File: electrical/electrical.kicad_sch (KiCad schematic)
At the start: 0 parts

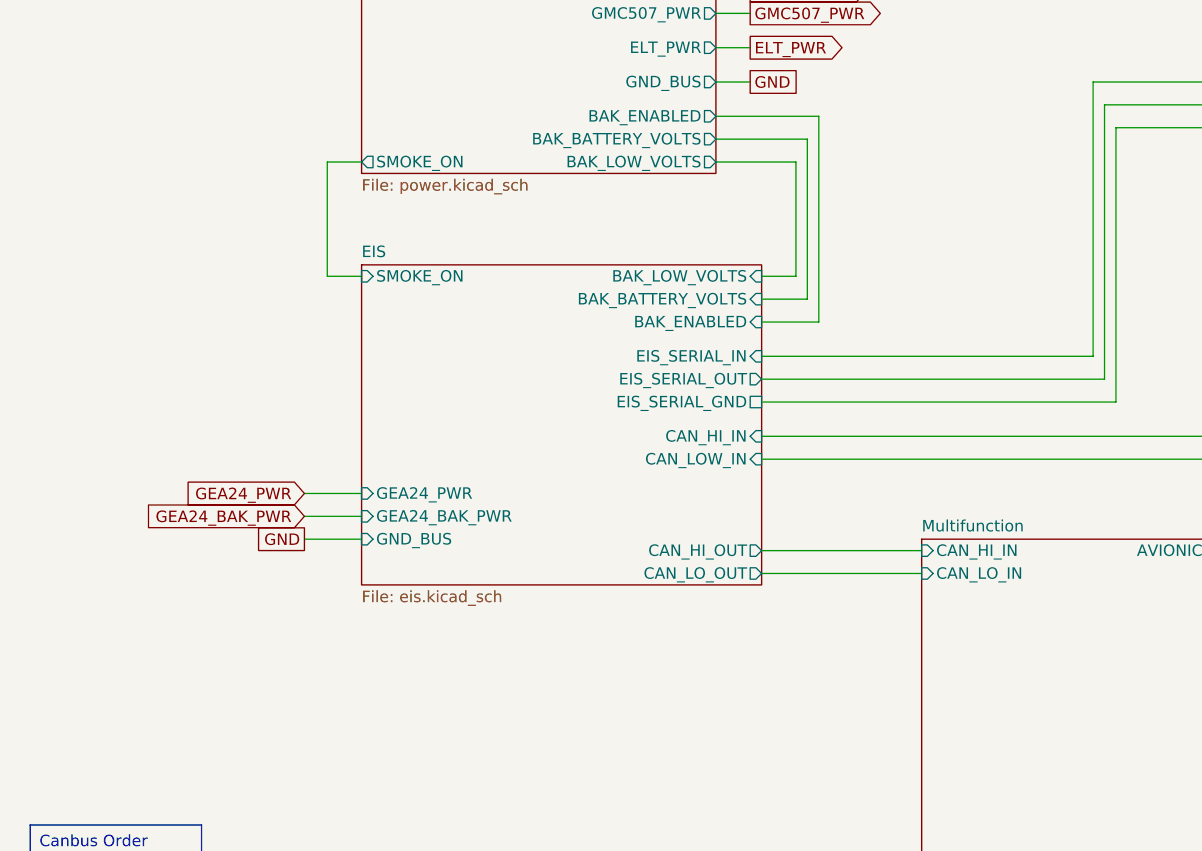
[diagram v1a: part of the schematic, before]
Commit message: Added Warning/Caution lights/buttons. Moved smoke on to GAD 27. Added glide button to GAD 27. Added lighting switched pots to GEA 24.
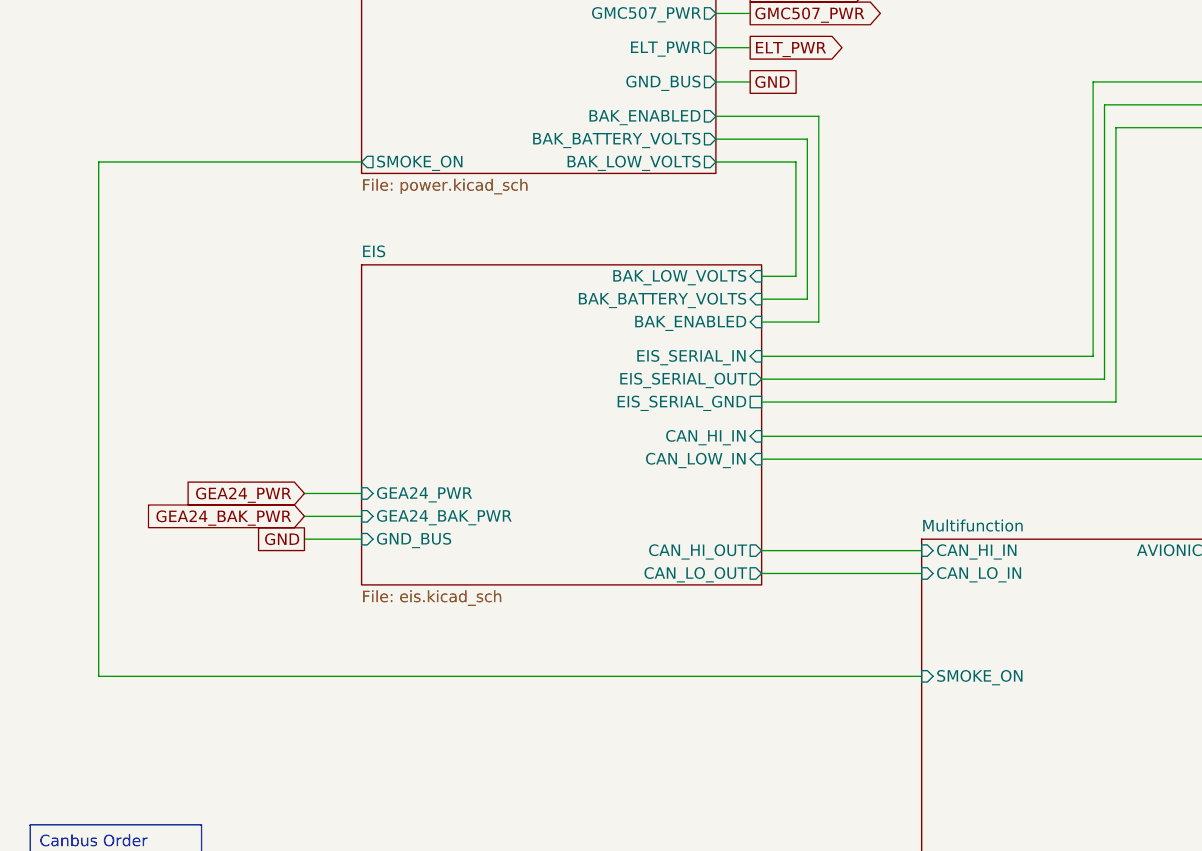
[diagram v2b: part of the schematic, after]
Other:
- sheet EIS ports: added none; removed SMOKE_ON
- sheet Multifunction ports: added SMOKE_ON; removed none
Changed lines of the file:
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@@
     (stroke (width 0) (type default))
   )
-  (wire (pts (xy 53.34 119.38) (xy 49.53 119.38))
+  (wire (pts (xy 24.13 119.38) (xy 53.34 119.38))
     (stroke (width 0) (type default))
   )
@@
     (stroke (width 0) (type default))
   )
-  (wire (pts (xy 49.53 119.38) (xy 49.53 132.08))
-    (stroke (width 0) (type default))
-  )
   (wire (pts (xy 134.62 110.49) (xy 173.99 110.49))
     (stroke (width 0) (type default))
@@
     (stroke (width 0) (type default))
   )
+  (wire (pts (xy 24.13 176.53) (xy 24.13 119.38))
+    (stroke (width 0) (type default))
+  )
   (wire (pts (xy 389.89 181.61) (xy 346.71 181.61))
     (stroke (width 0) (type default))
@@
     (stroke (width 0) (type default))
   )
+  (wire (pts (xy 115.57 176.53) (xy 24.13 176.53))
+    (stroke (width 0) (type default))
+  )
   (wire (pts (xy 92.71 87.63) (xy 96.52 87.63))
     (stroke (width 0) (type default))
@@
   )
   (wire (pts (xy 220.98 107.95) (xy 257.81 107.95))
-    (stroke (width 0) (type default))
-  )
-  (wire (pts (xy 49.53 132.08) (xy 53.34 132.08))
     (stroke (width 0) (type default))
   )
@@
       (effects (font (size 1.27 1.27)) (justify right))
     )
+    (pin "SMOKE_ON" input (at 115.57 176.53 180)
+      (effects (font (size 1.27 1.27)) (justify left))
+    )
     (instances
       (project "electrical"
@@
       (effects (font (size 1.27 1.27)) (justify right))
     )
-    (pin "SMOKE_ON" input (at 53.34 132.08 180)
-      (effects (font (size 1.27 1.27)) (justify left))
-    )
     (pin "EIS_SERIAL_OUT" output (at 97.79 143.51 0)

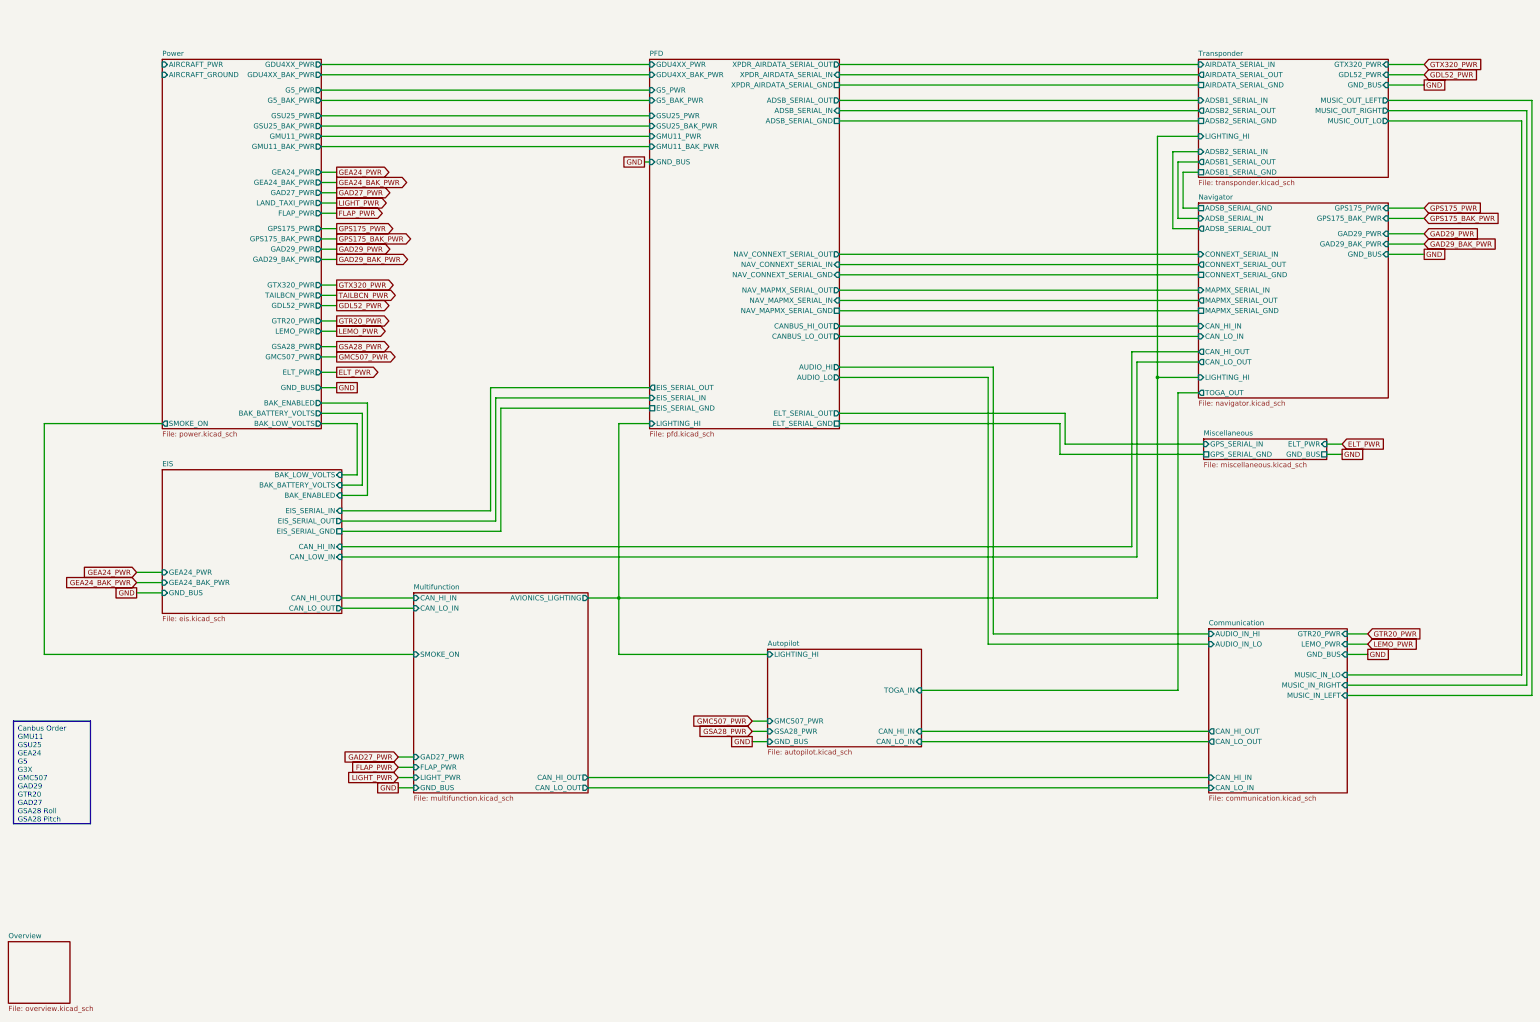
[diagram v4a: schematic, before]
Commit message: Updated electrical to not use IBBS. Also, added BT adapter and 3P3T switch.
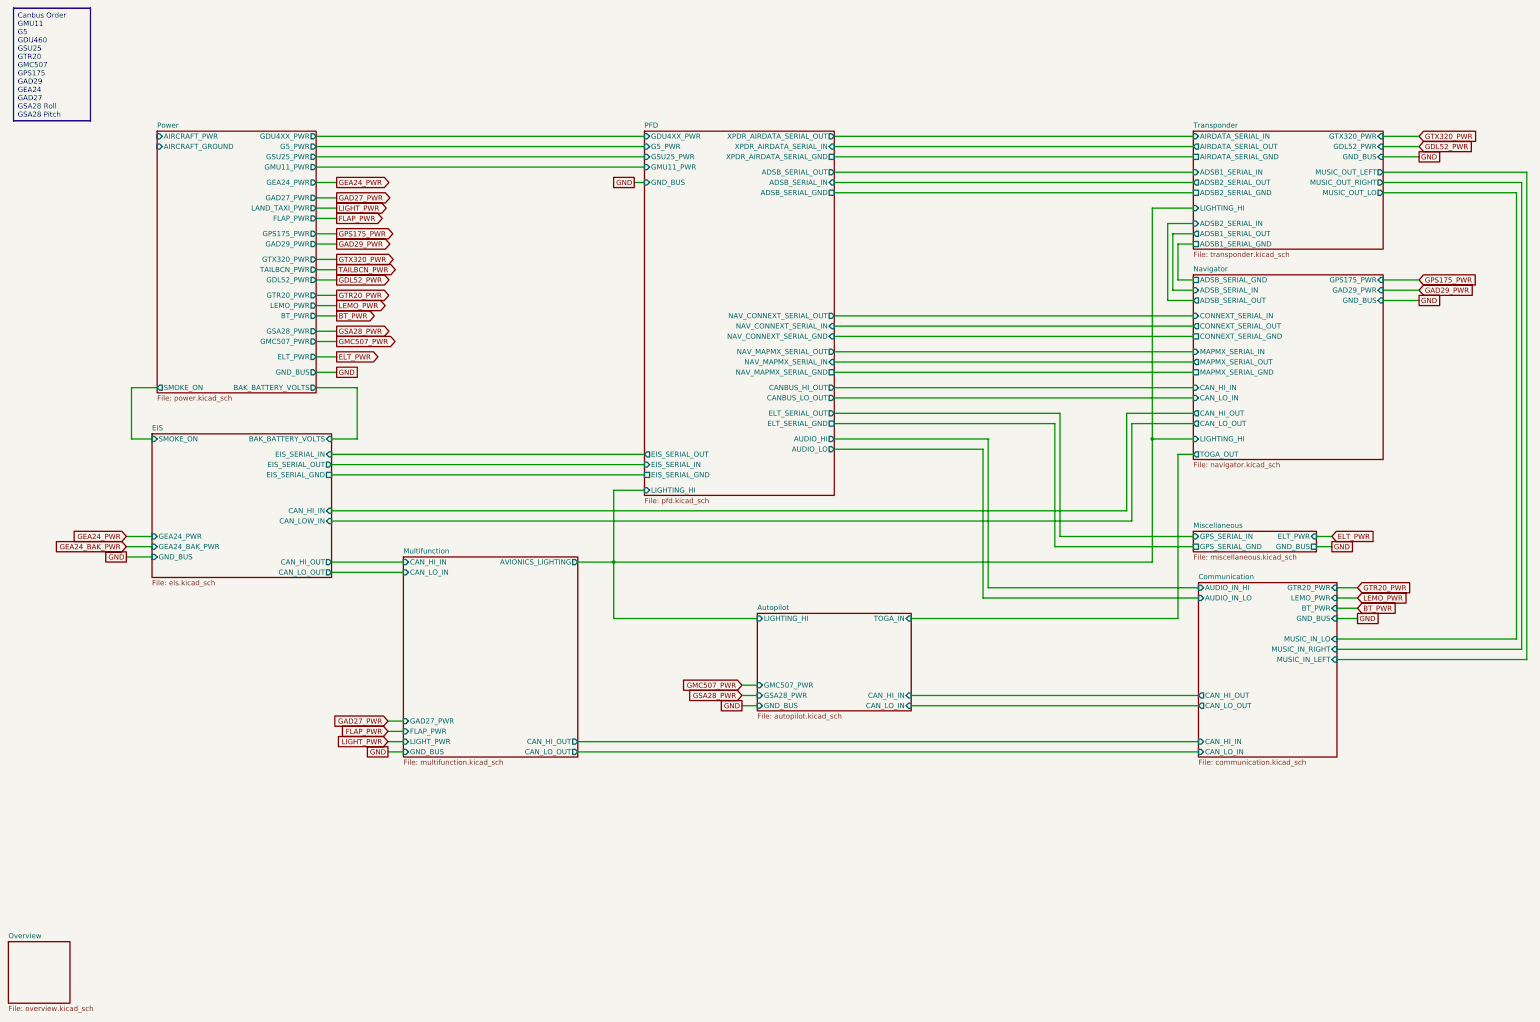
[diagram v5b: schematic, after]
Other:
- sheet Communication ports: added BT_PWR; removed none
- sheet EIS ports: added SMOKE_ON; removed BAK_ENABLED, BAK_LOW_VOLTS
- sheet Multifunction ports: added none; removed SMOKE_ON
- sheet Navigator ports: added none; removed GAD29_BAK_PWR, GPS175_BAK_PWR
- sheet PFD ports: added none; removed G5_BAK_PWR, GDU4XX_BAK_PWR, GMU11_BAK_PWR, GSU25_BAK_PWR
- sheet Power ports: added BT_PWR; removed BAK_ENABLED, BAK_LOW_VOLTS, G5_BAK_PWR, GAD29_BAK_PWR, GDU4XX_BAK_PWR, GEA24_BAK_PWR, GMU11_BAK_PWR, GPS175_BAK_PWR, GSU25_BAK_PWR

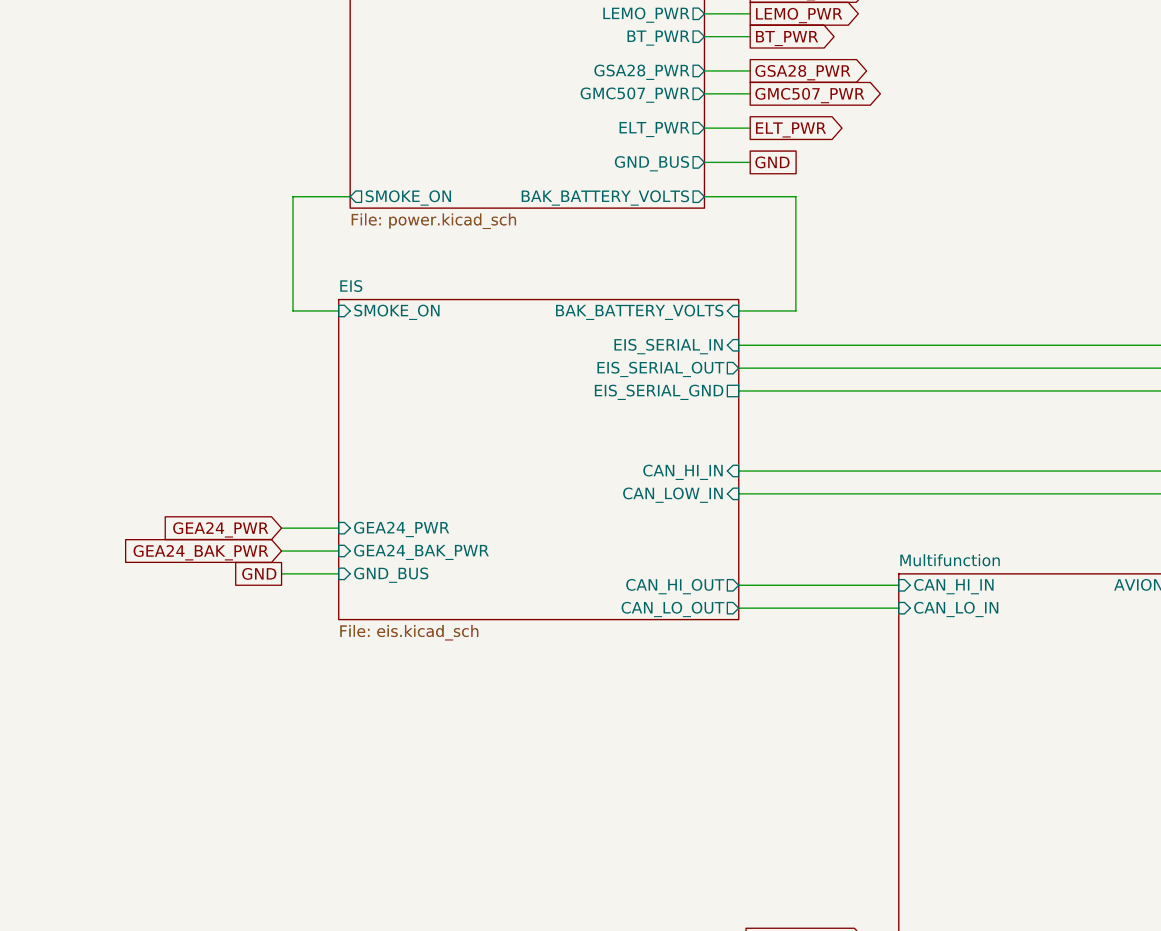
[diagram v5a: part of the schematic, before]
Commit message: Changed GTR CB to 7.5A. Added engine instrumentation. Added signal for fuel on.
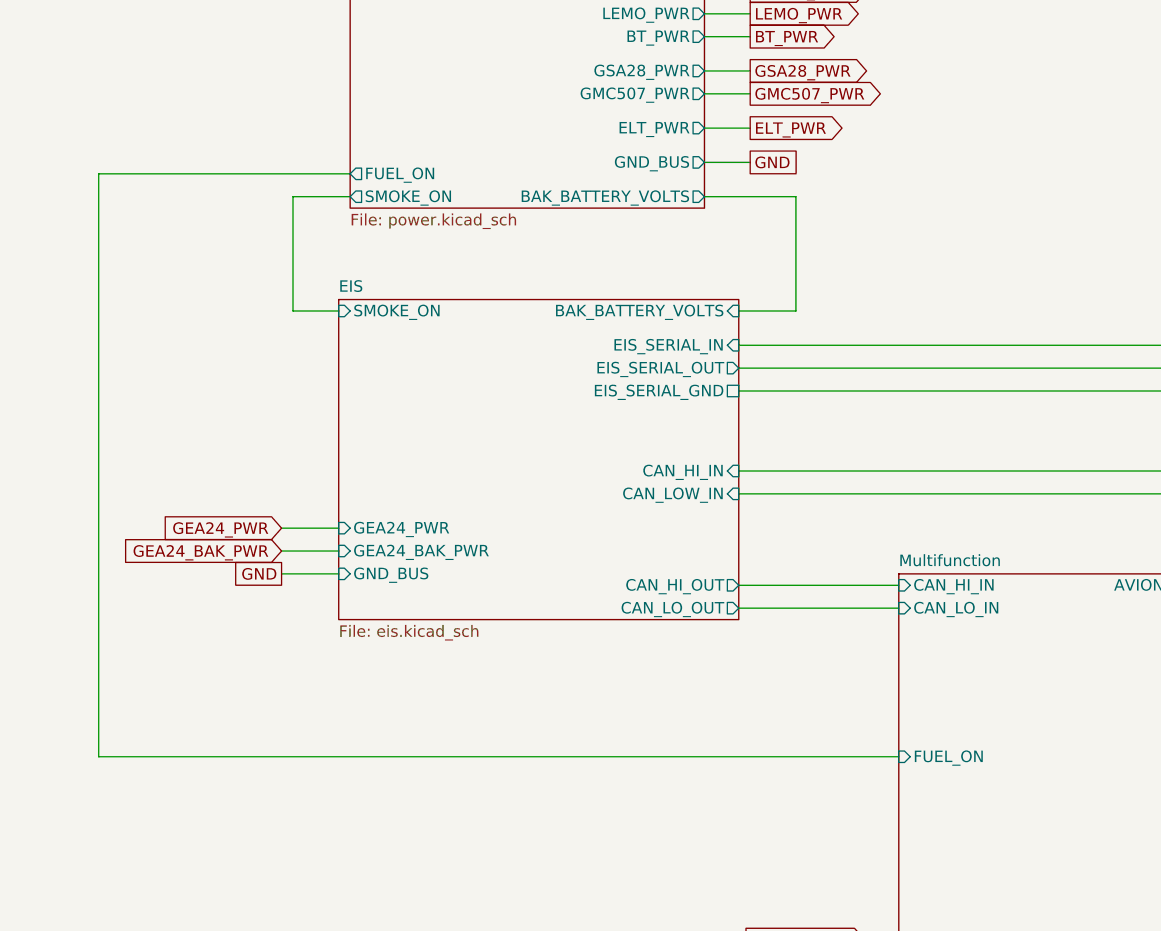
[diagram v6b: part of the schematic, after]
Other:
- sheet Multifunction ports: added FUEL_ON; removed none
- sheet Power ports: added FUEL_ON; removed none
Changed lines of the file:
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@@
   (title_block
     (title "Electrical Overview")
-    (date "2024-02-14")
-    (rev "0.9.3")
+    (date "2024-05-02")
+    (rev "0.9.4")
     (company "N877RV")
   )
@@
     (stroke (width 0) (type default))
   )
+  (wire (pts (xy 24.13 172.72) (xy 113.03 172.72))
+    (stroke (width 0) (type default))
+  )
   (wire (pts (xy 219.71 53.34) (xy 308.61 53.34))
     (stroke (width 0) (type default))
@@
     (stroke (width 0) (type default))
   )
+  (wire (pts (xy 24.13 107.95) (xy 24.13 172.72))
+    (stroke (width 0) (type default))
+  )
   (wire (pts (xy 339.09 149.86) (xy 342.9 149.86))
     (stroke (width 0) (type default))
@@
   )
   (wire (pts (xy 219.71 59.69) (xy 308.61 59.69))
+    (stroke (width 0) (type default))
+  )
+  (wire (pts (xy 52.07 107.95) (xy 24.13 107.95))
     (stroke (width 0) (type default))
   )
@@
       (effects (font (size 1.27 1.27)) (justify right))
     )
+    (pin "FUEL_ON" output (at 52.07 107.95 180)
+      (effects (font (size 1.27 1.27)) (justify left))
+    )
     (instances
       (project "electrical"
@@
       (effects (font (size 1.27 1.27)) (justify right))
     )
+    (pin "FUEL_ON" input (at 113.03 172.72 180)
+      (effects (font (size 1.27 1.27)) (justify left))
+    )
     (instances
